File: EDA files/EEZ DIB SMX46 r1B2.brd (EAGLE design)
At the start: 146 x 95 mm, 159 parts, among them IC1 STM32F030C6T6, IC2 74HC1G126GW,125, IC3 M24C32-WMN6P, IC4 LP2985-33DBVR, IC5 74HC2G04GW,125, IC6 OPA2170, K1 FTR-C1GA012G-B05, K10 FTR-C1GA012G-B05, K11 FTR-C1GA012G-B05, K12 FTR-C1GA012G-B05, K13 FTR-C1GA012G-B05, K14 FTR-C1GA012G-B05, K15 FTR-C1GA012G-B05, K16 FTR-C1GA012G-B05, K17 FTR-C1GA012G-B05, K18 FTR-C1GA012G-B05, K19 FTR-C1GA012G-B05, K2 FTR-C1GA012G-B05, K20 FTR-C1GA012G-B05, K21 FTR-C1GA012G-B05, K22 FTR-C1GA012G-B05, K23 FTR-C1GA012G-B05, K24 FTR-C1GA012G-B05, K3 FTR-C1GA012G-B05, K4 FTR-C1GA012G-B05, K5 FTR-C1GA012G-B05, K6 FTR-C1GA012G-B05, K7 FTR-C1GA012G-B05, K8 FTR-C1GA012G-B05, K9 FTR-C1GA012G-B05, Q1 2N7002, Q10 2N7002, Q11 2N7002, Q12 2N7002, Q13 2N7002, Q14 2N7002, Q15 2N7002, Q16 2N7002, Q17 2N7002, Q18 2N7002, Q19 2N7002, Q2 2N7002, Q20 2N7002, Q21 2N7002, Q22 2N7002, Q23 2N7002, Q24 2N7002, Q25 2N7002, Q3 2N7002, Q4 2N7002, Q5 2N7002, Q6 2N7002, Q7 2N7002, Q8 2N7002, Q9 2N7002, X1 N.C., X2 77317-104-28LF, X3 691327310016, X4 691327310016

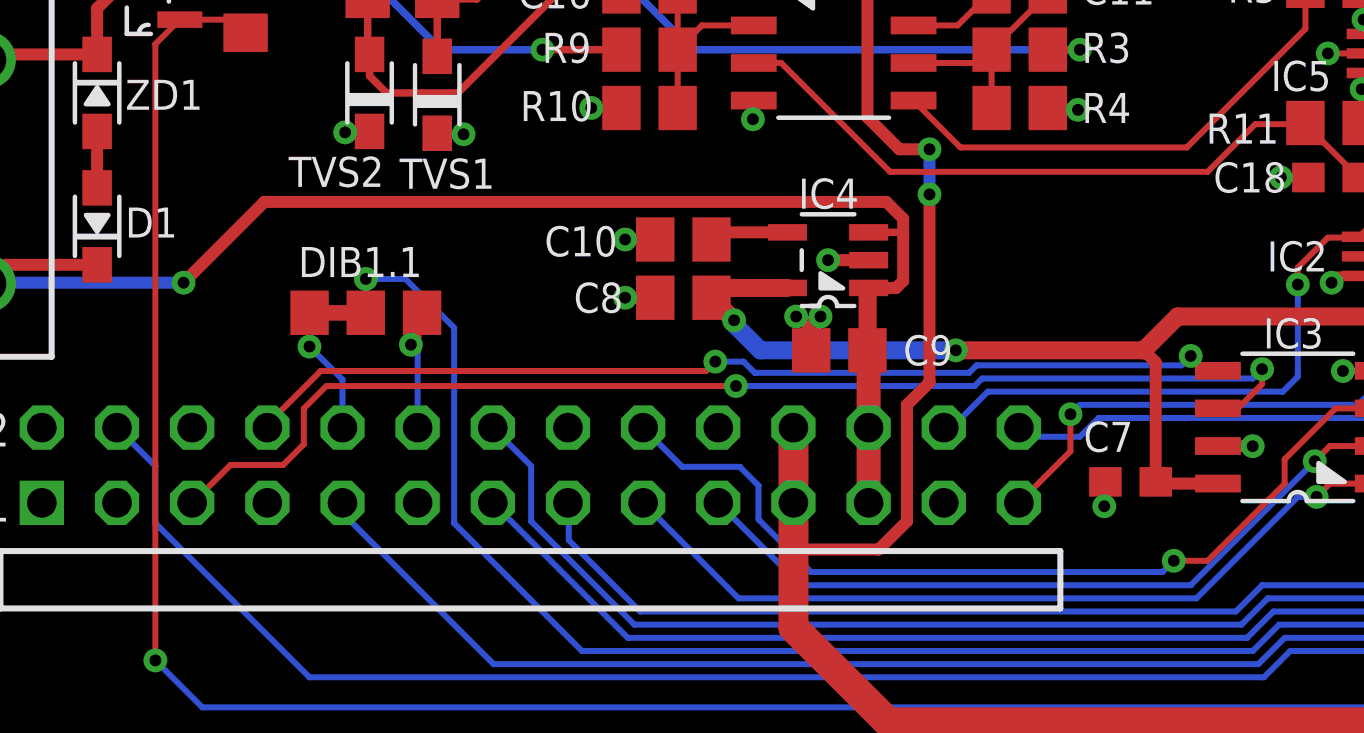
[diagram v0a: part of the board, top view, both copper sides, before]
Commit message: front panel labels update
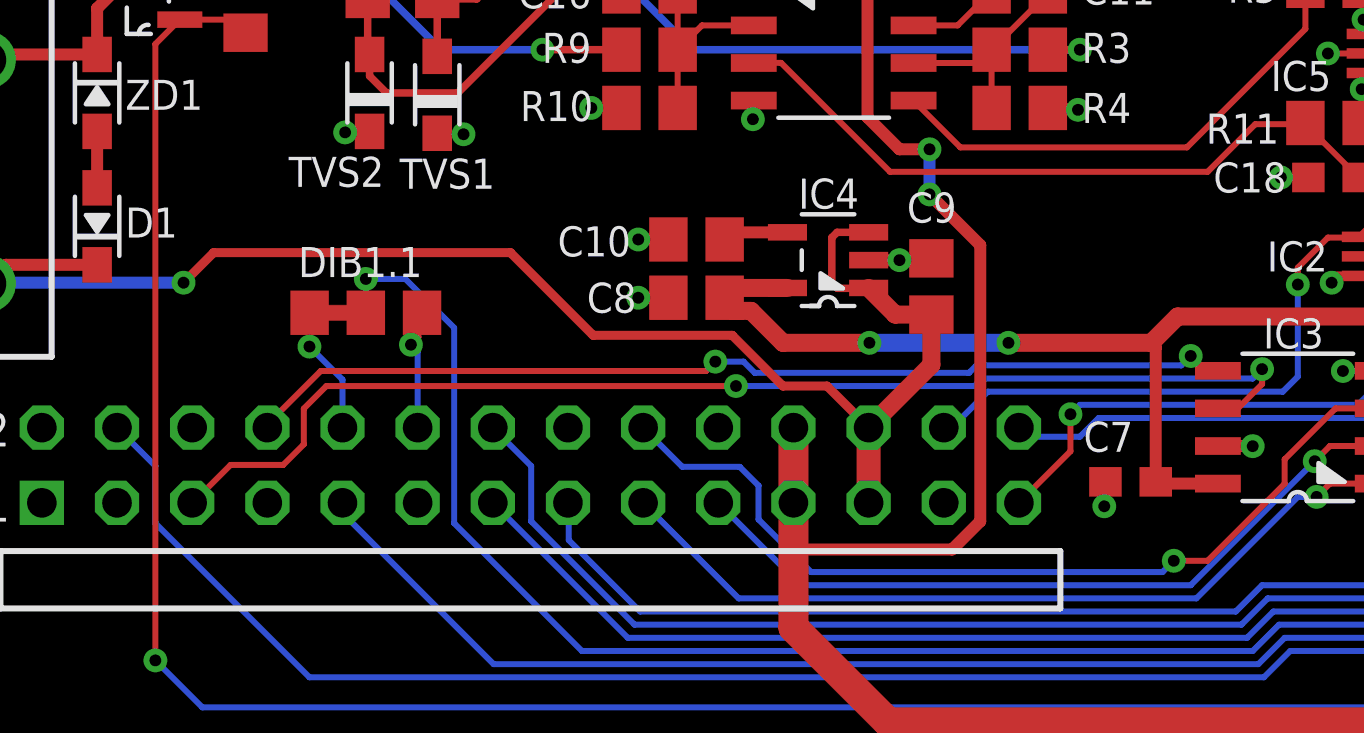
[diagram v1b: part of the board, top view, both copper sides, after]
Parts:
- C2, C9: value 4u7 -> 2u2
- IC6: value OPA2170 -> OPA2990IDR
- moved C9 3.79 mm to (84.6, 17.3), turned to 270 degrees
- moved C10 0.44 mm to (76.6, 18.9)
- moved C8 0.44 mm to (76.6, 16.9)
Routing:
- net +12V: track 720.9 -> 723.7 mm
- net +5V: track 48.2 -> 50.6 mm
- net +3V3: track 104.1 -> 103.5 mm
- net GND: track 132.9 -> 132.4 mm, vias 69 -> 67

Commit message: Gerbers update
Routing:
- net +12V: track 723.7 -> 732.5 mm

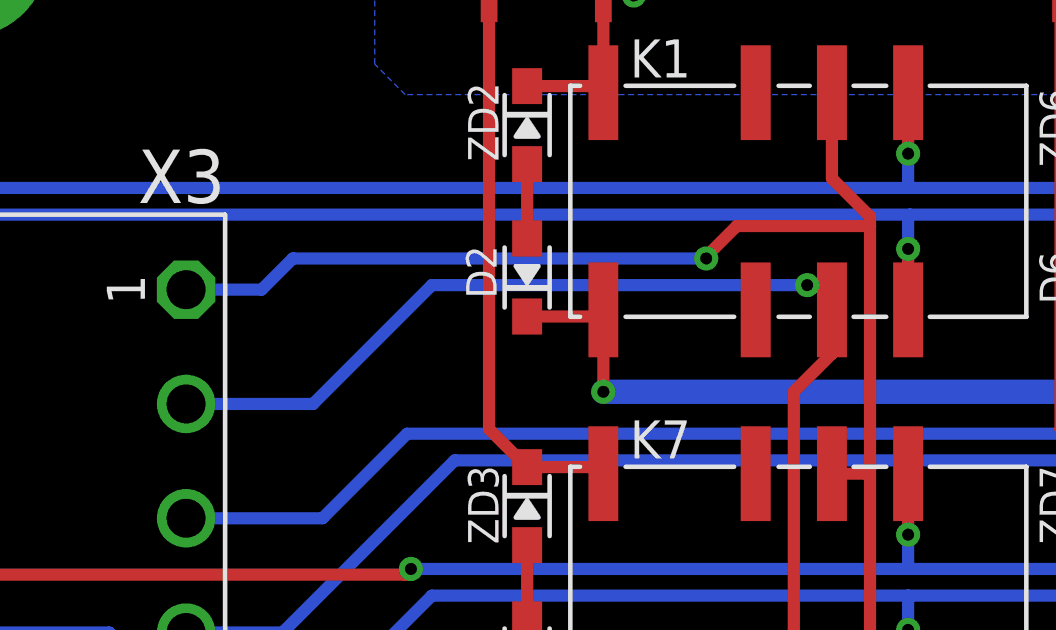
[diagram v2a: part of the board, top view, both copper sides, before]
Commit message: C6 value
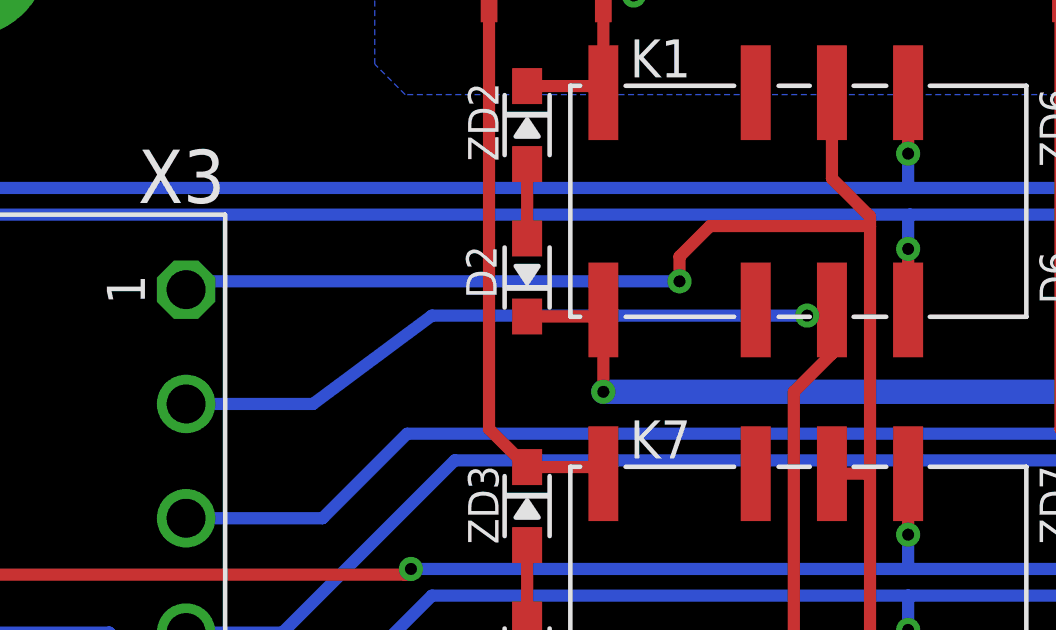
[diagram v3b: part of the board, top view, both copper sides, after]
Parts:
- C6: value 1u -> 2u2
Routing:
- net N$1: track 65.7 -> 64.4 mm
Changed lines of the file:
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@@
 <attribute name="VALUE" x="108.839" y="18.415" size="1.016" layer="27" ratio="10" rot="R90" align="center"/>
 </element>
-<element name="C6" library="rcl" package="C0805" value="1u" x="116.459" y="14.986" smashed="yes">
+<element name="C6" library="rcl" package="C0805" value="2u2" x="116.459" y="14.986" smashed="yes">
 <attribute name="NAME" x="114.4905" y="15.367" size="1.016" layer="25" ratio="10" rot="R180"/>
 <attribute name="VALUE" x="115.6335" y="14.5415" size="1.016" layer="27" ratio="10"/>
@@
 <contactref element="X3" pad="2"/>
 <wire x1="18.35" y1="74.525" x2="22.582" y2="74.525" width="0.4064" layer="16"/>
-<wire x1="22.582" y1="74.525" x2="26.543" y2="78.486" width="0.4064" layer="16"/>
-<wire x1="26.543" y1="78.486" x2="39.0525" y2="78.486" width="0.4064" layer="16"/>
-<via x="39.0525" y="78.486" extent="1-16" drill="0.4" shape="octagon"/>
-<wire x1="39.0525" y1="78.486" x2="39.878" y2="78.486" width="0.4064" layer="1"/>
-<wire x1="39.878" y1="78.486" x2="39.878" y2="77.66" width="0.4064" layer="1"/>
+<wire x1="22.582" y1="74.525" x2="26.543" y2="77.47" width="0.4064" layer="16"/>
+<wire x1="26.543" y1="77.47" x2="39.0525" y2="77.47" width="0.4064" layer="16"/>
+<via x="39.0525" y="77.47" extent="1-16" drill="0.4" shape="octagon"/>
+<wire x1="39.0525" y1="77.47" x2="39.878" y2="77.47" width="0.4064" layer="1"/>
+<wire x1="39.878" y1="77.47" x2="39.878" y2="77.66" width="0.4064" layer="1"/>
 </signal>
 <signal name="N$2">
@@
 <wire x1="39.878" y1="46.8" x2="39.878" y2="48.8315" width="0.4064" layer="1"/>
 <contactref element="X3" pad="1"/>
-<wire x1="18.35" y1="78.335" x2="20.8675" y2="78.335" width="0.4064" layer="16"/>
-<wire x1="20.8675" y1="78.335" x2="21.9075" y2="79.375" width="0.4064" layer="16"/>
-<wire x1="21.9075" y1="79.375" x2="35.687" y2="79.375" width="0.4064" layer="16"/>
-<via x="35.687" y="79.375" extent="1-16" drill="0.4" shape="octagon"/>
-<wire x1="35.687" y1="79.375" x2="35.687" y2="79.4385" width="0.4064" layer="1"/>
-<wire x1="35.687" y1="79.4385" x2="36.703" y2="80.4545" width="0.4064" layer="1"/>
-<wire x1="36.703" y1="80.4545" x2="41.148" y2="80.4545" width="0.4064" layer="1"/>
+<via x="34.798" y="78.613" extent="1-16" drill="0.4" shape="octagon"/>
+<wire x1="34.798" y1="78.613" x2="34.798" y2="79.4385" width="0.4064" layer="1"/>
+<wire x1="34.798" y1="79.4385" x2="35.814" y2="80.4545" width="0.4064" layer="1"/>
+<wire x1="35.814" y1="80.4545" x2="41.148" y2="80.4545" width="0.4064" layer="1"/>
+<wire x1="34.798" y1="78.613" x2="18.628" y2="78.613" width="0.4064" layer="16"/>
+<wire x1="18.628" y1="78.613" x2="18.35" y2="78.335" width="0.4064" layer="16"/>
 </signal>
 <signal name="N$6">
